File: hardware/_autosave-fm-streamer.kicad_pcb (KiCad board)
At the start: 4 copper layers, 40 x 60 mm, 56 parts, among them J1 USB_A, U1 ESP32_DevKit_V1_DOIT, U2 PCM1772PWR, U3 SI4721

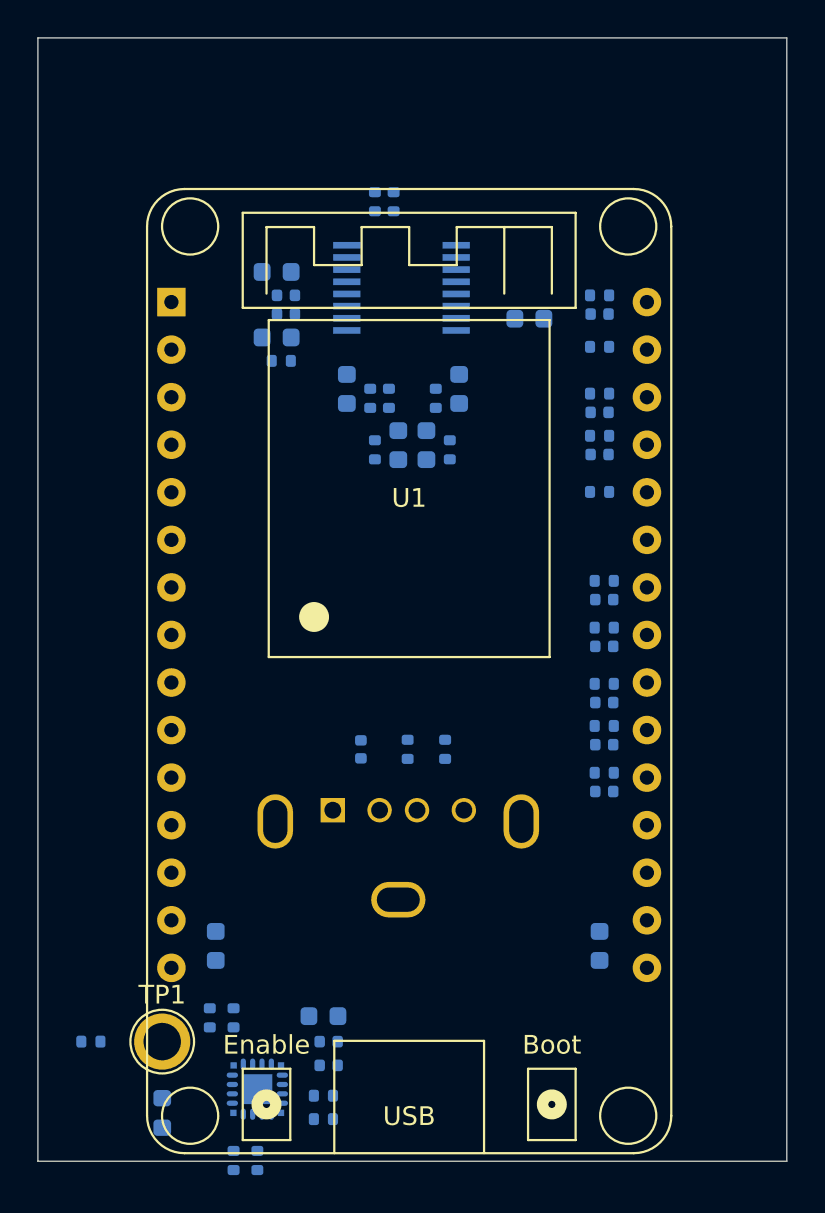
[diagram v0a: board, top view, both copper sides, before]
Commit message: rough placement and routing complete, needs cleanup
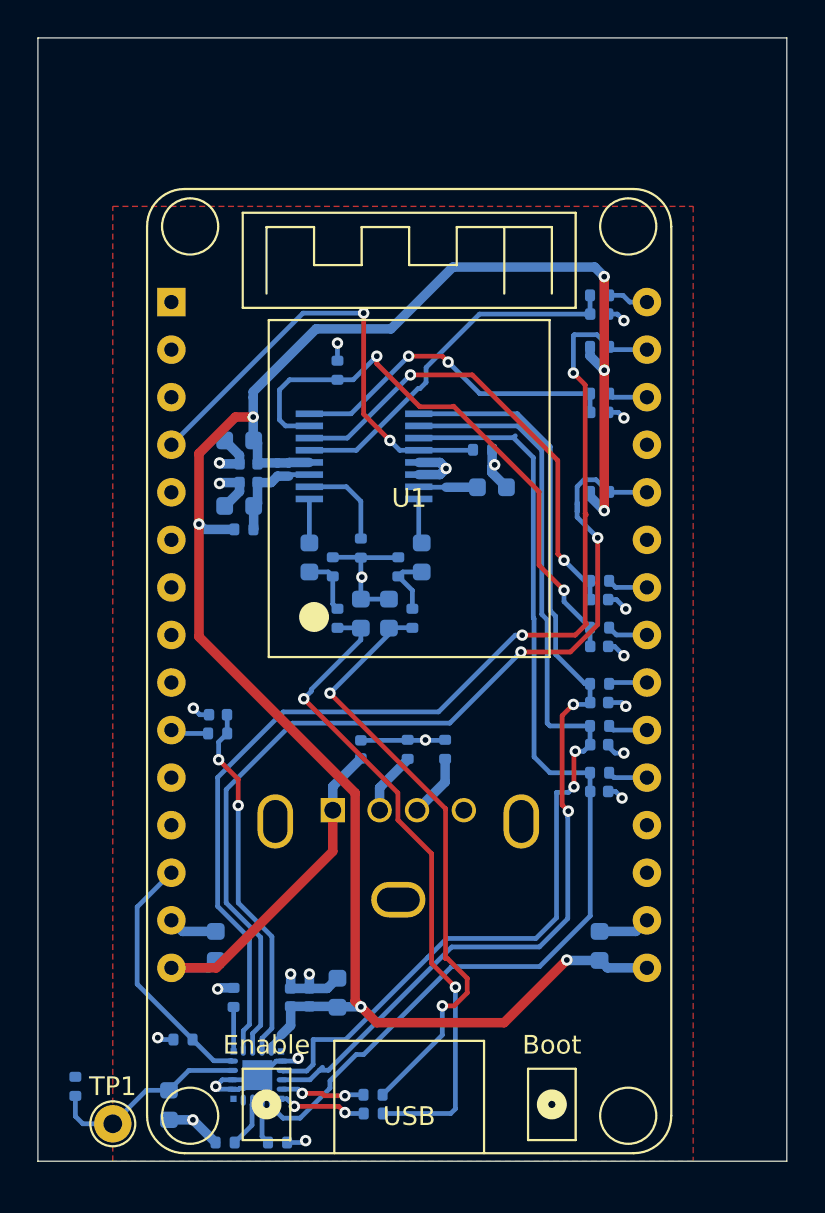
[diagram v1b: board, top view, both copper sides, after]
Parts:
- TP1: footprint TestPoint:TestPoint_Plated_Hole_D2.0mm -> TestPoint:TestPoint_THTPad_D2.0mm_Drill1.0mm
- moved R7 25.9 mm to (189.6, 107.2), turned to 180 degrees
- moved C7 24.7 mm to (189.6, 106.2), turned to 180 degrees
- moved R15 14.1 mm to (203.8, 92.0), turned to 0 degrees
- moved C12 9.22 mm to (190.8, 95.0)
- moved C13 9.22 mm to (191.2, 93.8)
- moved C14 9.22 mm to (190.8, 91.5)
- moved C15 9.22 mm to (191.2, 92.8)
- moved C16 9.22 mm to (204.2, 94.0)
- moved C19 9.22 mm to (200.5, 97.8)
- moved C20 9.22 mm to (194.5, 97.8)
- moved C22 9.22 mm to (198.8, 100.8)
- moved C23 9.22 mm to (197.2, 100.8)
- moved R13 9.22 mm to (191.0, 96.2)
- moved R16 9.22 mm to (196.0, 87.8)
- moved R24 9.22 mm to (199.2, 98.2)
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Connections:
- C11 pad 1: SPI_CS -> SPI_~CS~
- R11 pad 1: SPI_CS -> SPI_~CS~
- U1 pad 10: DAC_~RST~ -> /RAD_CLK_R
- U1 pad 13: Net-(U1-Pad13) -> RADIO_~RST~
- U1 pad 27: /RAD_CLK_R -> Net-(U1-Pad27)
- U1 pad 4: Net-(U1-Pad4) -> DAC_~RST~
- U1 pad 8: RADIO_~RST~ -> Net-(U1-Pad8)
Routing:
- net +3V3: track 0.00 -> 106.5 mm, vias 0 -> 7
- net I2C_SCK: track 0.00 -> 58.6 mm, vias 0 -> 2
- net I2S_DCLK: track 0.00 -> 56.0 mm
- net GND: track 0.00 -> 55.3 mm, vias 0 -> 23
- net I2S_DATA: track 0.00 -> 54.6 mm, vias 0 -> 2
- net I2S_WCLK: track 0.00 -> 54.3 mm, vias 0 -> 2
- net I2C_SDA: track 0.00 -> 50.8 mm, vias 0 -> 2
- net AUDIO_L: track 0.00 -> 35.5 mm, vias 0 -> 2
- net AUDIO_R: track 0.00 -> 32.9 mm, vias 0 -> 2
- net SPI_~CS~: track 0.00 -> 30.6 mm, vias 0 -> 2
- net DAC_~RST~: track 0.00 -> 25.2 mm, vias 0 -> 2
- net SPI_CLK: track 0.00 -> 24.9 mm, vias 0 -> 2
- net RADIO_REFCLK: track 0.00 -> 19.5 mm, vias 0 -> 2
- net SPI_MOSI: track 0.00 -> 19.5 mm
- net +5V: track 0.00 -> 19.3 mm
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- added copper zone on F.Cu, net GND
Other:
- copper layers 4 -> 2
